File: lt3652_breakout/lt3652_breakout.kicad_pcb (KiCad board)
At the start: 2 copper layers, 25.4 x 25.4 mm, 4 parts, among them P1 CONN_01X06, P2 CONN_01X06, P3 GND, U1 LT3652

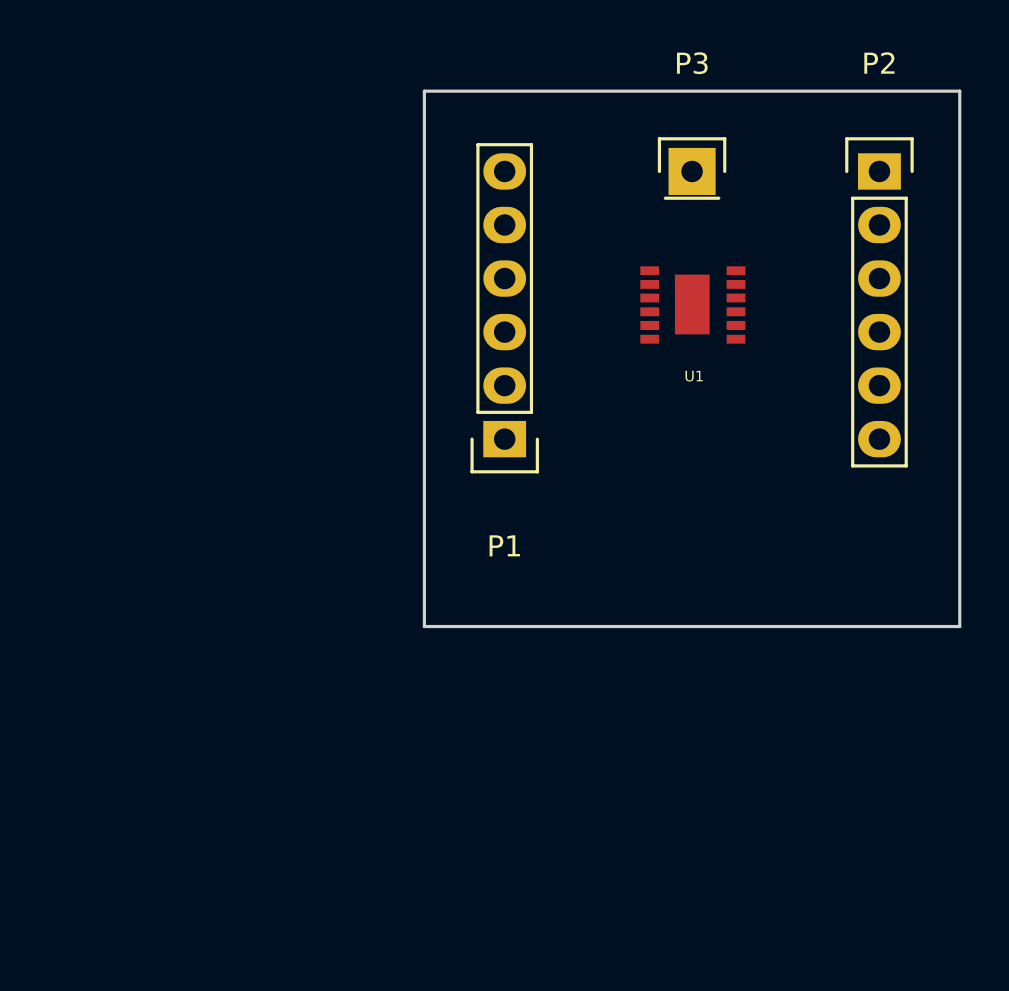
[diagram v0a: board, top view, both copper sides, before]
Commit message: WIP on LT3652 breakout
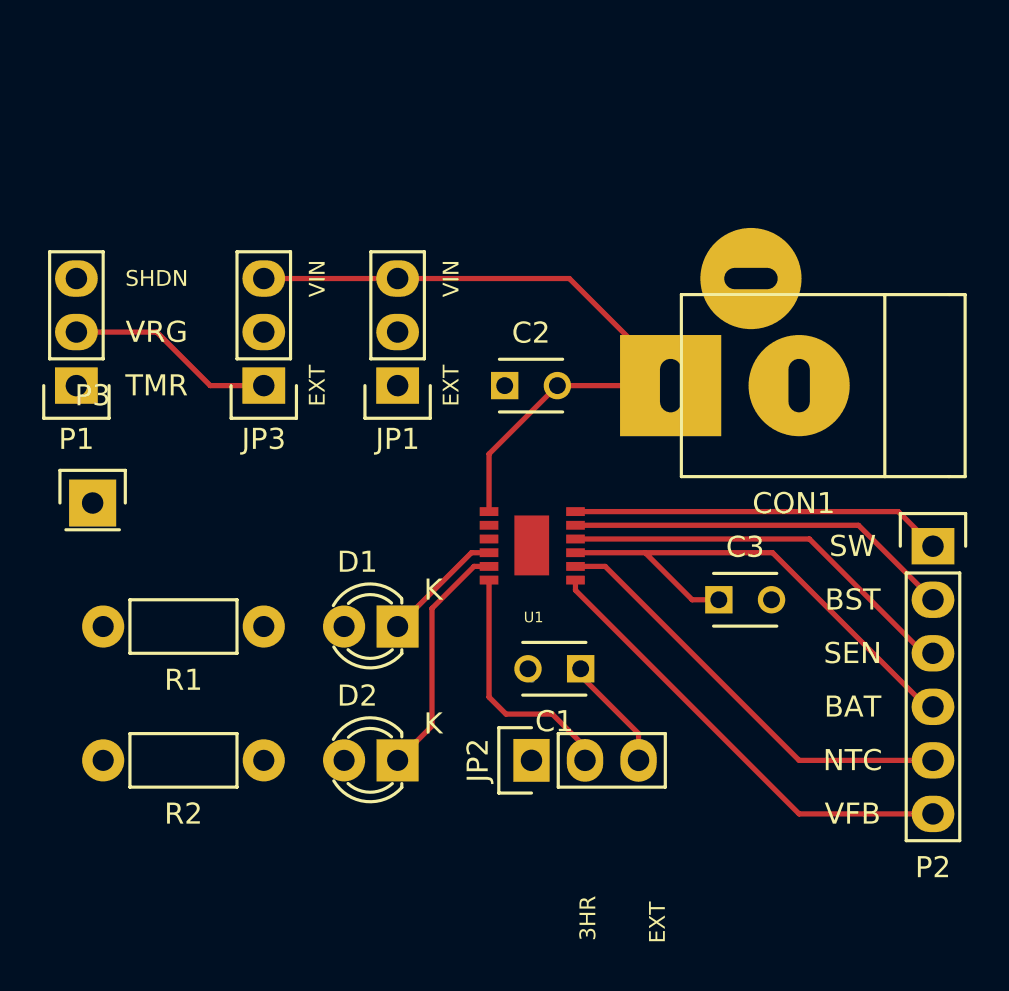
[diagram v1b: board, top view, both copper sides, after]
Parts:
- added C1: 0.68uF, Capacitors_ThroughHole:C_Disc_D3_P2.5, F.Cu at (149.7, 113.8)
- added C2: 10uF, Capacitors_ThroughHole:C_Disc_D3_P2.5, F.Cu at (146.1, 100.3)
- added C3: 10uF, Capacitors_ThroughHole:C_Disc_D3_P2.5, F.Cu at (156.2, 110.5)
- added CON1: SLR PNL, Connect:JACK_ALIM, F.Cu at (160.0, 100.3)
- added D1: 3mm GRN, LEDs:LED-3MM, F.Cu at (141.0, 111.8)
- added D2: 3mm RED, LEDs:LED-3MM, F.Cu at (141.0, 118.1)
- added JP1: SHDN OPT, Pin_Headers:Pin_Header_Straight_1x03, F.Cu at (141.0, 100.3)
- added JP2: TIMER OPT, Pin_Headers:Pin_Header_Straight_1x03, F.Cu at (147.3, 118.1)
- added JP3: VREG OPT, Pin_Headers:Pin_Header_Straight_1x03, F.Cu at (134.6, 100.3)
- added R1: 220, Resistors_ThroughHole:Resistor_Horizontal_RM7mm, F.Cu at (134.6, 111.8)
- added R2: 220, Resistors_ThroughHole:Resistor_Horizontal_RM7mm, F.Cu at (134.6, 118.1)
- P1: value CONN_01X06 -> OUT LEFT; footprint Pin_Headers:Pin_Header_Straight_1x06 -> Pin_Headers:Pin_Header_Straight_1x03
- P2: value CONN_01X06 -> OUT RIGHT
- moved P3 32.5 mm to (126.5, 105.9)
- moved P1 20.5 mm to (125.7, 100.3)
- moved P2 18.0 mm to (166.4, 108.0)
- moved U1 13.7 mm to (147.3, 108.0)
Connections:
- net /BAT renamed Net-(C3-Pad1)
- net /BOOST renamed Net-(P2-Pad2)
- net /NTC renamed Net-(P2-Pad5)
- net /SENSE renamed Net-(P2-Pad3)
- net /SW renamed Net-(P2-Pad1)
- net /VFB renamed Net-(P2-Pad6)
- net Net-(P3-Pad1) renamed GND
- P1 pad 1: /TIMER -> Net-(JP2-Pad1)
- P1 pad 2: /FAULT -> Net-(JP3-Pad1)
- P1 pad 3: /CHRG -> Net-(JP1-Pad1)
- U1 pad 1: /VIN -> VIN
- U1 pad 2: /VIN_REG -> VREG
- U1 pad 3: /SHDN -> SHDN
- U1 pad 4: /CHRG -> Net-(D1-Pad1)
- U1 pad 5: /FAULT -> Net-(D2-Pad1)
- U1 pad 6: /TIMER -> TIMER
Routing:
- net VIN: track 0.00 -> 35.8 mm
- net Net-(C3-Pad1): track 0.00 -> 24.4 mm
- net Net-(P2-Pad6): track 0.00 -> 21.8 mm
- net Net-(P2-Pad5): track 0.00 -> 20.8 mm
- net Net-(P2-Pad3): track 0.00 -> 19.2 mm
- net Net-(P2-Pad2): track 0.00 -> 18.4 mm
- net Net-(P2-Pad1): track 0.00 -> 17.6 mm
- net TIMER: track 0.00 -> 11.7 mm
- net Net-(D2-Pad1): track 0.00 -> 11.4 mm
- net Net-(JP3-Pad1): track 0.00 -> 9.94 mm
- net Net-(D1-Pad1): track 0.00 -> 5.79 mm
- net Net-(C1-Pad1): track 0.00 -> 4.86 mm
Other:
- board outline removed
- board text added: "3HR"
- board text added: "BAT"
- board text added: "BST"
- board text added: "EXT"
- board text added: "NTC"
- board text added: "SEN"
- board text added: "SHDN"
- board text added: "SW"
- board text added: "TMR"
- board text added: "VFB"
- board text added: "VIN"
- board text added: "VRG"

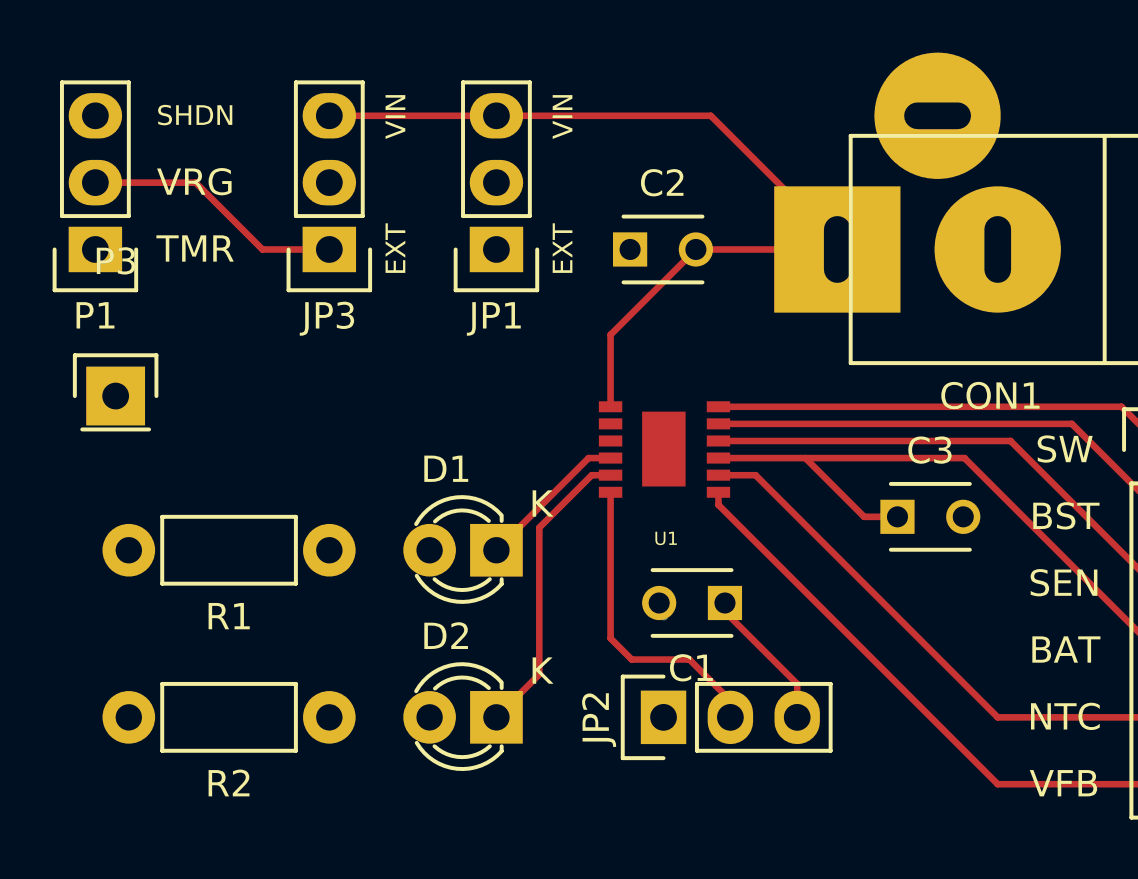
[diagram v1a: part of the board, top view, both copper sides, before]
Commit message: WIP on LT3652 breakout
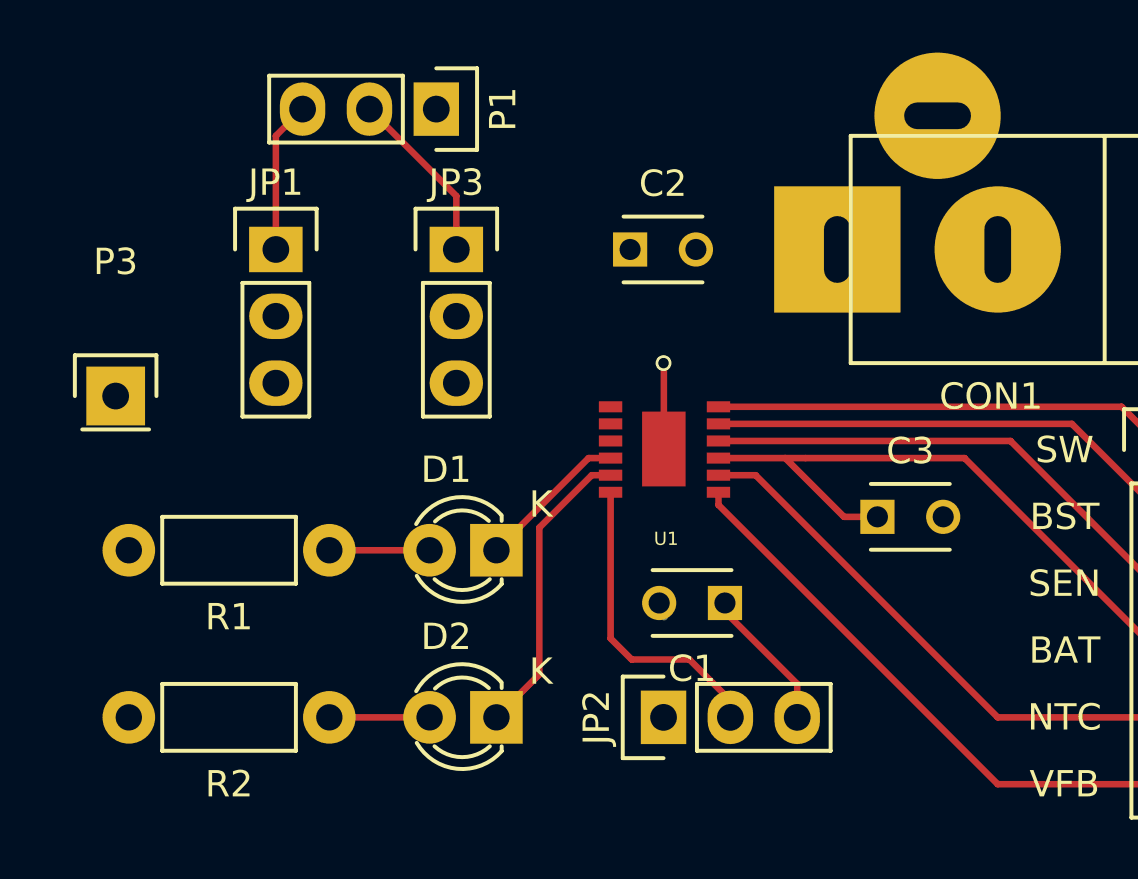
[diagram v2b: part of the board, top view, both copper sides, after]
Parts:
- P1: value OUT LEFT -> (none)
- moved P1 14.0 mm to (138.7, 95.0), turned to 270 degrees
- moved JP1 8.38 mm to (132.6, 100.3), turned to 0 degrees
- moved JP3 4.83 mm to (139.4, 100.3), turned to 0 degrees
- moved C3 0.76 mm to (155.4, 110.5)
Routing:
- net VIN: track 35.8 -> 1.80 mm
- net Net-(JP1-Pad1): track 0.00 -> 5.75 mm
- net Net-(D2-Pad2): track 0.00 -> 3.81 mm
- net Net-(D1-Pad2): track 0.00 -> 3.81 mm
- net GND: track 0.04 -> 3.31 mm, vias 0 -> 1
- net Net-(JP3-Pad1): track 9.94 -> 6.70 mm
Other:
- board text removed: "SHDN"
- board text removed: "TMR"
- board text removed: "VIN"
- board text removed: "VRG"

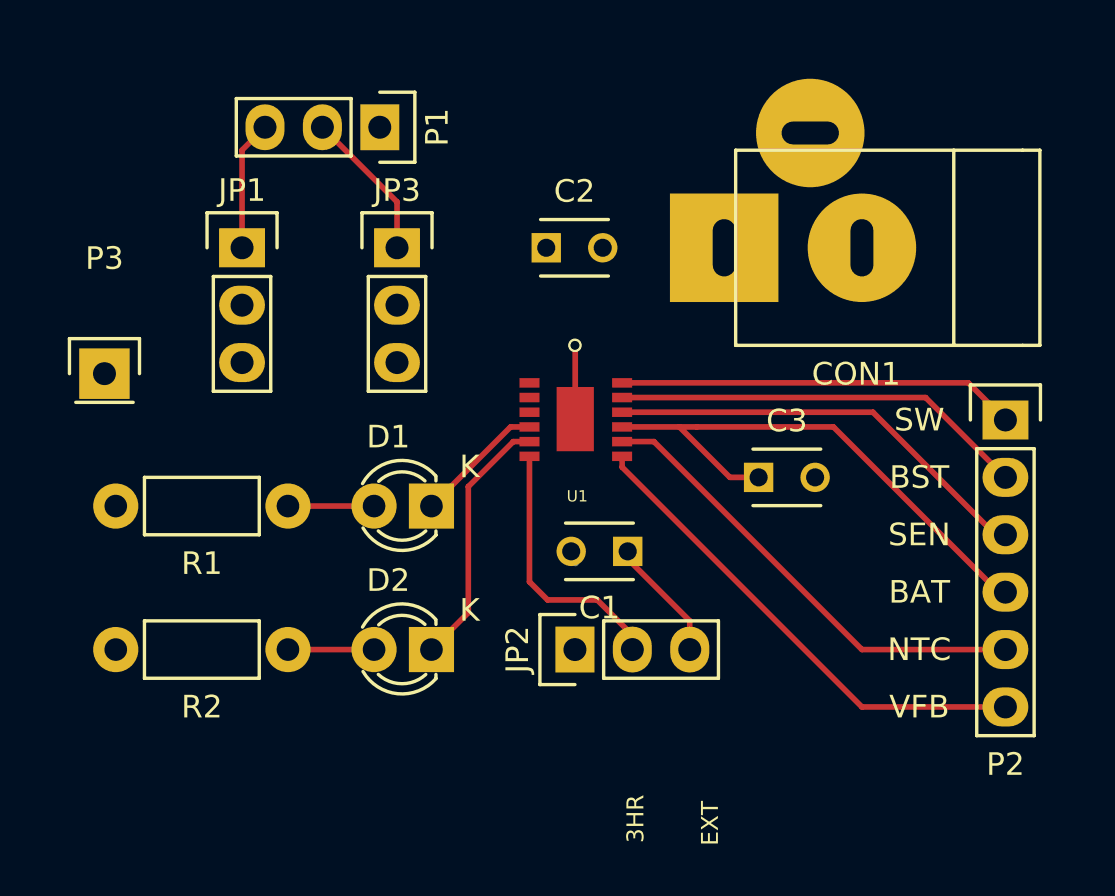
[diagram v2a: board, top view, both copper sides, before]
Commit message: LT3652 Breakout Rev 0.1
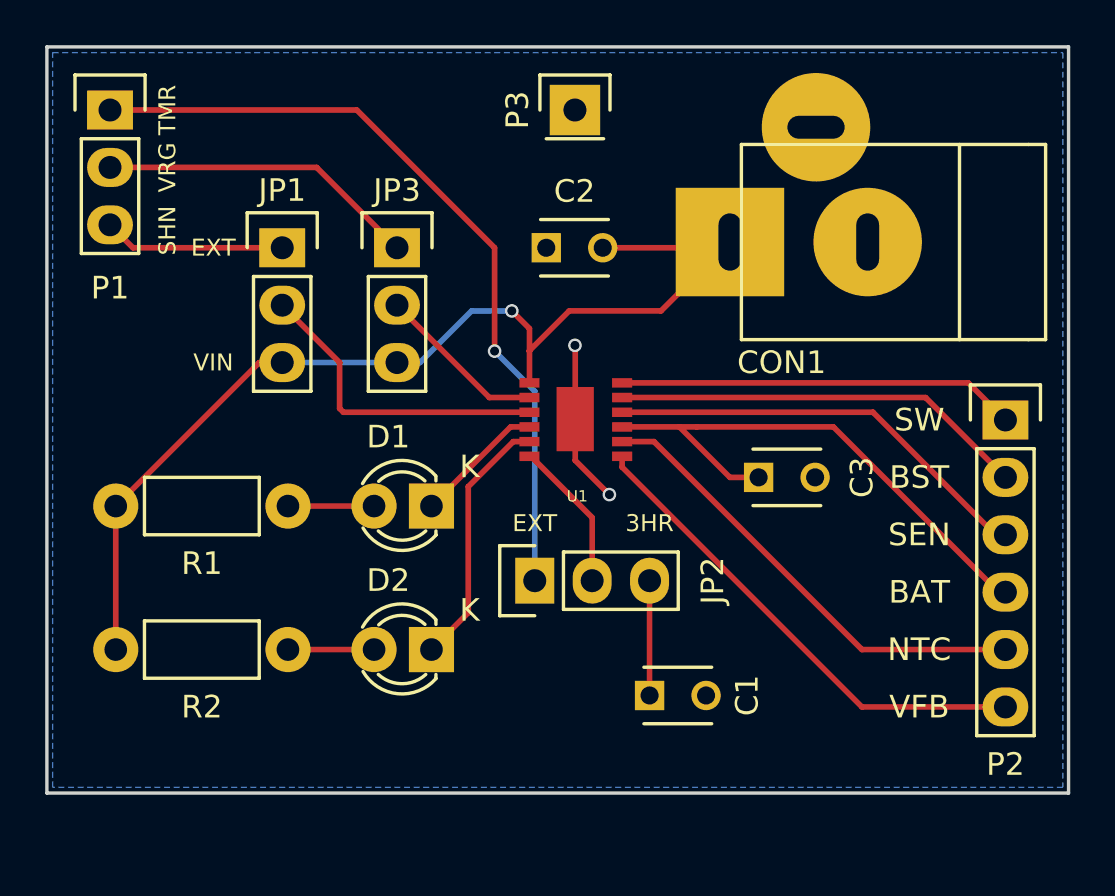
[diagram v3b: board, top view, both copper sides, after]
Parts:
- D1: value 3mm GRN -> (none)
- D2: value 3mm RED -> (none)
- P2: value OUT RIGHT -> (none)
- moved P3 23.9 mm to (147.3, 94.2)
- moved P1 12.0 mm to (126.7, 94.2), turned to 0 degrees
- moved C1 6.45 mm to (150.6, 120.1), turned to 0 degrees
- moved JP2 3.53 mm to (145.5, 115.1)
- moved JP1 1.78 mm to (134.4, 100.3)
- moved CON1 0.36 mm to (160.3, 100.1)
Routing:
- net VIN: track 1.80 -> 48.6 mm, vias 0 -> 1
- net Net-(JP2-Pad1): track 0.00 -> 35.0 mm, vias 0 -> 1
- net SHDN: track 0.00 -> 14.1 mm
- net VREG: track 0.00 -> 7.55 mm
- net Net-(JP3-Pad1): track 6.70 -> 14.2 mm
- net TIMER: track 11.7 -> 6.69 mm
- net GND: track 3.31 -> 7.24 mm, vias 1 -> 2
- net Net-(JP1-Pad1): track 5.75 -> 8.04 mm
- added copper zone on B.Cu, net GND
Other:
- board outline added: 45.2 x 33 mm
- board text added: "Crappy LT3652 Breakout Board Rev 0.1 malcolmspiterionline@gmail.com"
- board text added: "SHN"
- board text added: "TMR"
- board text added: "VIN"
- board text added: "VRG"
